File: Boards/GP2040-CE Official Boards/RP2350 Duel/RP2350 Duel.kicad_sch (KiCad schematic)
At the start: 28 parts, among them U1 W25Q128JVS, U2 RP2350B, Y1 SiT8008xx-7x-xxE

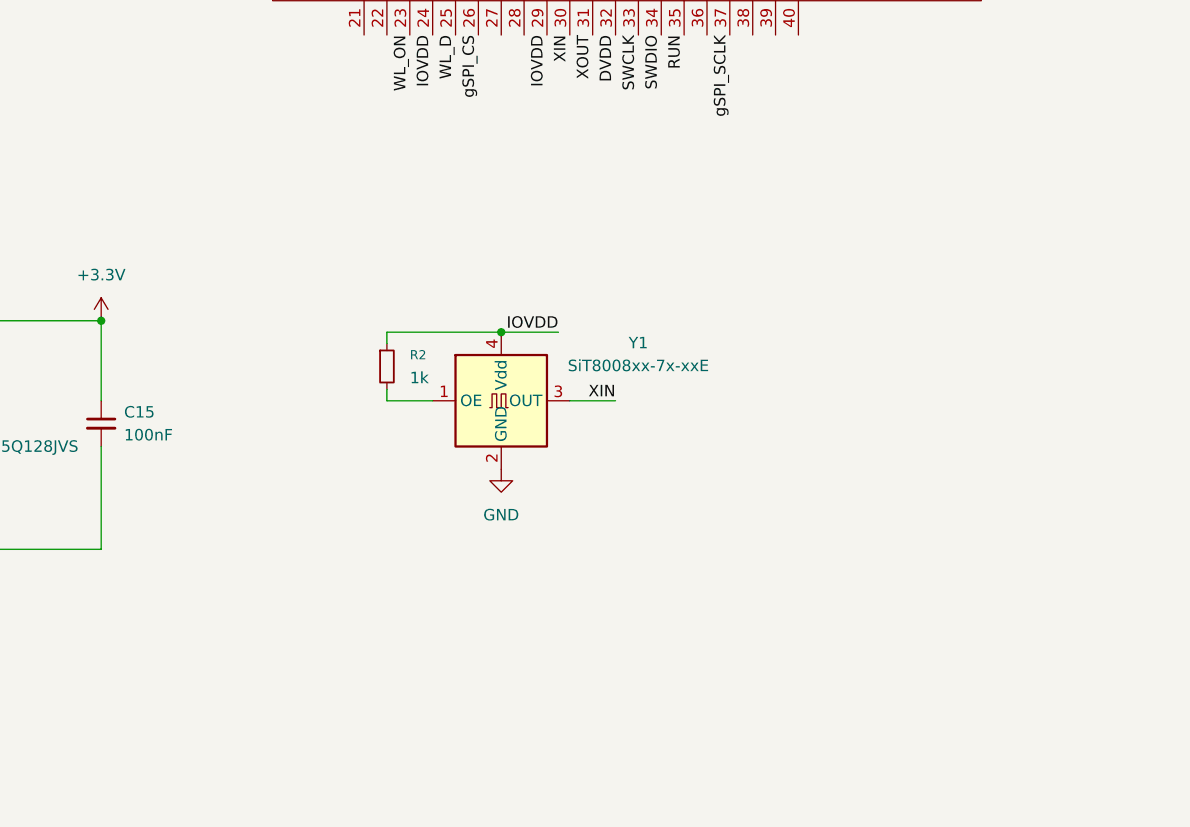
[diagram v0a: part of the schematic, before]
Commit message: adding new libraries
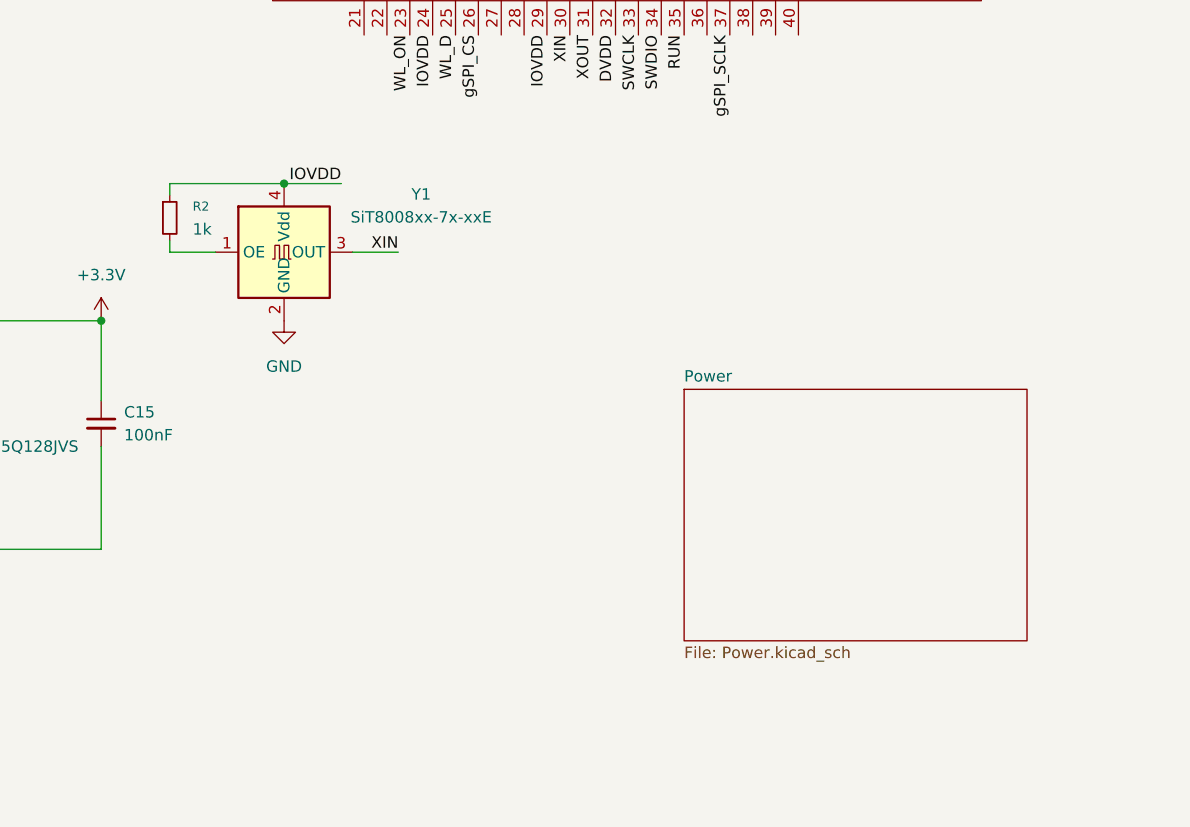
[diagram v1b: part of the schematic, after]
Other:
- added sheet Power (Power.kicad_sch)
- moved on the sheet: R2, Y1
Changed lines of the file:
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@@
 	)
 	(junction
-		(at 107.95 129.54)
+		(at 83.82 113.03)
 		(diameter 0)
 		(color 0 0 0 0)
@@
 	(wire
 		(pts
-			(xy 120.65 137.16) (xy 115.57 137.16)
+			(xy 96.52 120.65) (xy 91.44 120.65)
 		)
 		(stroke
@@
 	(wire
 		(pts
-			(xy 95.25 137.16) (xy 100.33 137.16)
+			(xy 71.12 120.65) (xy 76.2 120.65)
 		)
 		(stroke
@@
 	(wire
 		(pts
-			(xy 95.25 130.81) (xy 95.25 129.54)
+			(xy 71.12 114.3) (xy 71.12 113.03)
 		)
 		(stroke
@@
 	(wire
 		(pts
-			(xy 114.3 129.54) (xy 107.95 129.54)
+			(xy 90.17 113.03) (xy 83.82 113.03)
 		)
 		(stroke
@@
 	(wire
 		(pts
-			(xy 95.25 135.89) (xy 95.25 137.16)
+			(xy 71.12 119.38) (xy 71.12 120.65)
 		)
 		(stroke
@@
 	(wire
 		(pts
-			(xy 95.25 129.54) (xy 107.95 129.54)
+			(xy 71.12 113.03) (xy 83.82 113.03)
 		)
 		(stroke
@@
 	)
 	(label "XIN"
-		(at 120.65 137.16 180)
+		(at 96.52 120.65 180)
 		(effects
 			(font
@@
 	)
 	(label "IOVDD"
-		(at 114.3 129.54 180)
+		(at 90.17 113.03 180)
 		(effects
 			(font
@@
 	(symbol
 		(lib_id "Device:R_Small")
-		(at 95.25 133.35 0)
+		(at 71.12 116.84 0)
 		(unit 1)
 		(body_style 1)
@@
 		(fields_autoplaced yes)
 		(property "Reference" "R2"
-			(at 97.79 132.0799 0)
+			(at 73.66 115.5699 0)
 			(show_name no)
 			(do_not_autoplace no)
@@
 		)
 		(property "Value" "1k"
-			(at 97.79 134.6199 0)
+			(at 73.66 118.1099 0)
 			(show_name no)
 			(do_not_autoplace no)
@@
 		)
 		(property "Footprint" ""
-			(at 95.25 133.35 0)
+			(at 71.12 116.84 0)
 			(hide yes)
 			(show_name no)
@@
 		)
 		(property "Datasheet" ""
-			(at 95.25 133.35 0)
+			(at 71.12 116.84 0)
 			(hide yes)
 			(show_name no)
@@
 		)
 		(property "Description" "Resistor, small symbol"
-			(at 95.25 133.35 0)
+			(at 71.12 116.84 0)
 			(hide yes)
 			(show_name no)
@@
 	(symbol
 		(lib_id "power:GND")
-		(at 107.95 144.78 0)
+		(at 83.82 128.27 0)
 		(unit 1)
 		(body_style 1)
@@
 		(fields_autoplaced yes)
 		(property "Reference" "#PWR019"
-			(at 107.95 151.13 0)
+			(at 83.82 134.62 0)
 			(hide yes)
 			(show_name no)
@@
 		)
 		(property "Value" "GND"
-			(at 107.95 149.86 0)
+			(at 83.82 133.35 0)
 			(show_name no)
 			(do_not_autoplace no)
@@
 		)
 		(property "Footprint" ""
-			(at 107.95 144.78 0)
+			(at 83.82 128.27 0)
 			(hide yes)
 			(show_name no)
@@
 		)
 		(property "Datasheet" ""
-			(at 107.95 144.78 0)
+			(at 83.82 128.27 0)
 			(hide yes)
 			(show_name no)
@@
 		)
 		(property "Description" "Power symbol creates a global label with name \"GND\" , ground"
-			(at 107.95 144.78 0)
+			(at 83.82 128.27 0)
 			(hide yes)
 			(show_name no)
@@
 	(symbol
 		(lib_id "Oscillator:SiT8008xx-7x-xxE")
-		(at 107.95 137.16 0)
+		(at 83.82 120.65 0)
 		(unit 1)
 		(body_style 1)
@@
 		(fields_autoplaced yes)
 		(property "Reference" "Y1"
-			(at 123.19 130.7398 0)
+			(at 99.06 114.2298 0)
 			(show_name no)
 			(do_not_autoplace no)
@@
 		)
 		(property "Value" "SiT8008xx-7x-xxE"
-			(at 123.19 133.2798 0)
+			(at 99.06 116.7698 0)
 			(show_name no)
 			(do_not_autoplace no)
@@
 		)
 		(property "Footprint" "Oscillator:Oscillator_SMD_SiT_PQFN-4Pin_2.0x1.6mm"
-			(at 107.95 137.16 0)
+			(at 83.82 120.65 0)
 			(hide yes)
 			(show_name no)
@@
 		)
 		(property "Datasheet" "https://www.sitime.com/support/resource-library/datasheets/sit8008-datasheet"
-			(at 107.95 137.16 0)
+			(at 83.82 120.65 0)
 			(hide yes)
 			(show_name no)
@@
 		)
 		(property "Description" "SiTime Low Power Mems programmable oscillator, 1MHz to 110MHz, PQFN-4, 2.0x1.6mm (with output enable pin)"
-			(at 107.95 137.16 0)
+			(at 83.82 120.65 0)
 			(hide yes)
 			(show_name no)
@@
 				)
 			)
+		)
+	)
+	(sheet
+		(at 128.27 135.89)
+		(size 38.1 27.94)
+		(exclude_from_sim no)
+		(in_bom yes)
+		(on_board yes)
+		(dnp no)
+		(fields_autoplaced yes)
+		(stroke
+			(width 0.1524)
+			(type solid)
+		)
+		(fill
+			(color 0 0 0 0)
+		)
+		(property "Sheetname" "Power"
+			(at 128.27 135.1784 0)
+			(show_name no)
+			(do_not_autoplace no)
+			(effects
+				(font
+					(size 1.27 1.27)
+				)
+				(justify left bottom)
+			)
+		)
+		(property "Sheetfile" "Power.kicad_sch"
+			(at 128.27 164.4146 0)
+			(show_name no)
+			(do_not_autoplace no)
+			(effects
+				(font
+					(size 1.27 1.27)
+				)
+				(justify left top)
+			)
+		)
+		(instances
+			(project "RP2350 Duel"
+				(path "/9569aed4-f877-407f-b337-4ee93294723e"
+					(page "2")
+				)
+			)
